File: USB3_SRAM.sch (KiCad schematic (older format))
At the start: 33 parts

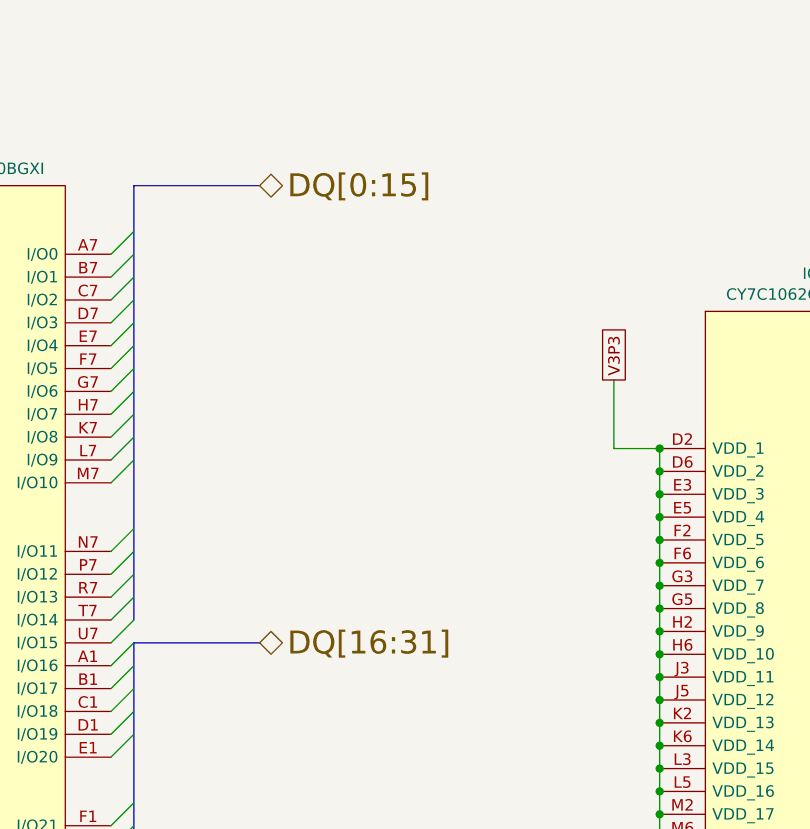
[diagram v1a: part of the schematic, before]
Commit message: Added nets for fx3 usb3 cct from fpga
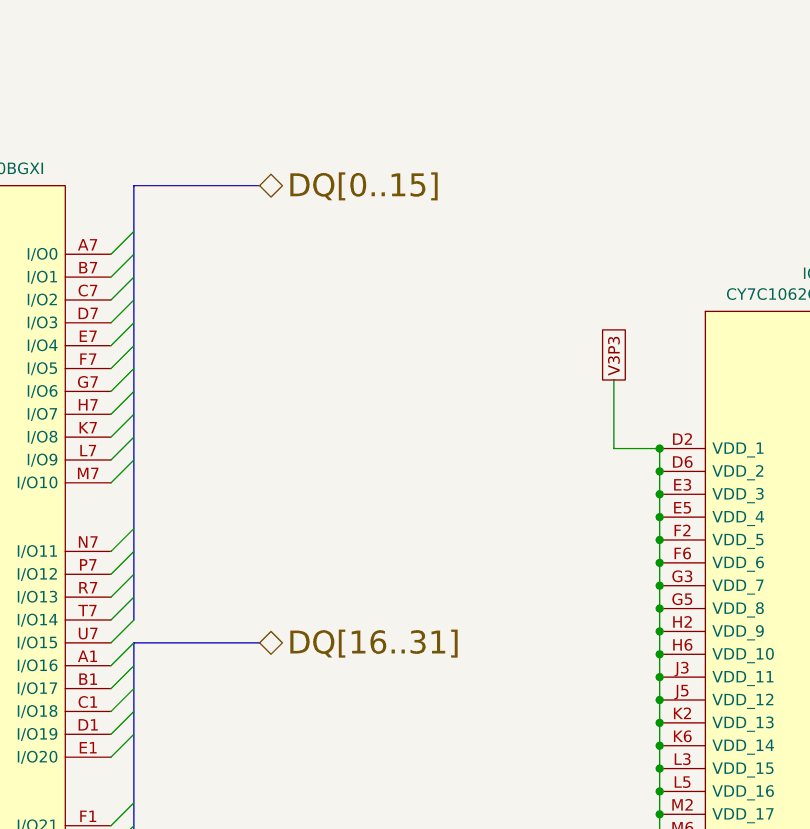
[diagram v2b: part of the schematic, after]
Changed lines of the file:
@@
 $Descr A4 11693 8268
 encoding utf-8
-Sheet 9 22
+Sheet 15 22
 Title ""
 Date ""
@@
 	6800 3700 7350 3700
 Text HLabel 7350 1700 2    100  BiDi ~ 0
-DQ[0:15]
+DQ[0..15]
 Text HLabel 7350 3700 2    100  BiDi ~ 0
-DQ[16:31]
+DQ[16..31]
 $Comp
 L power:GNDD #PWR?

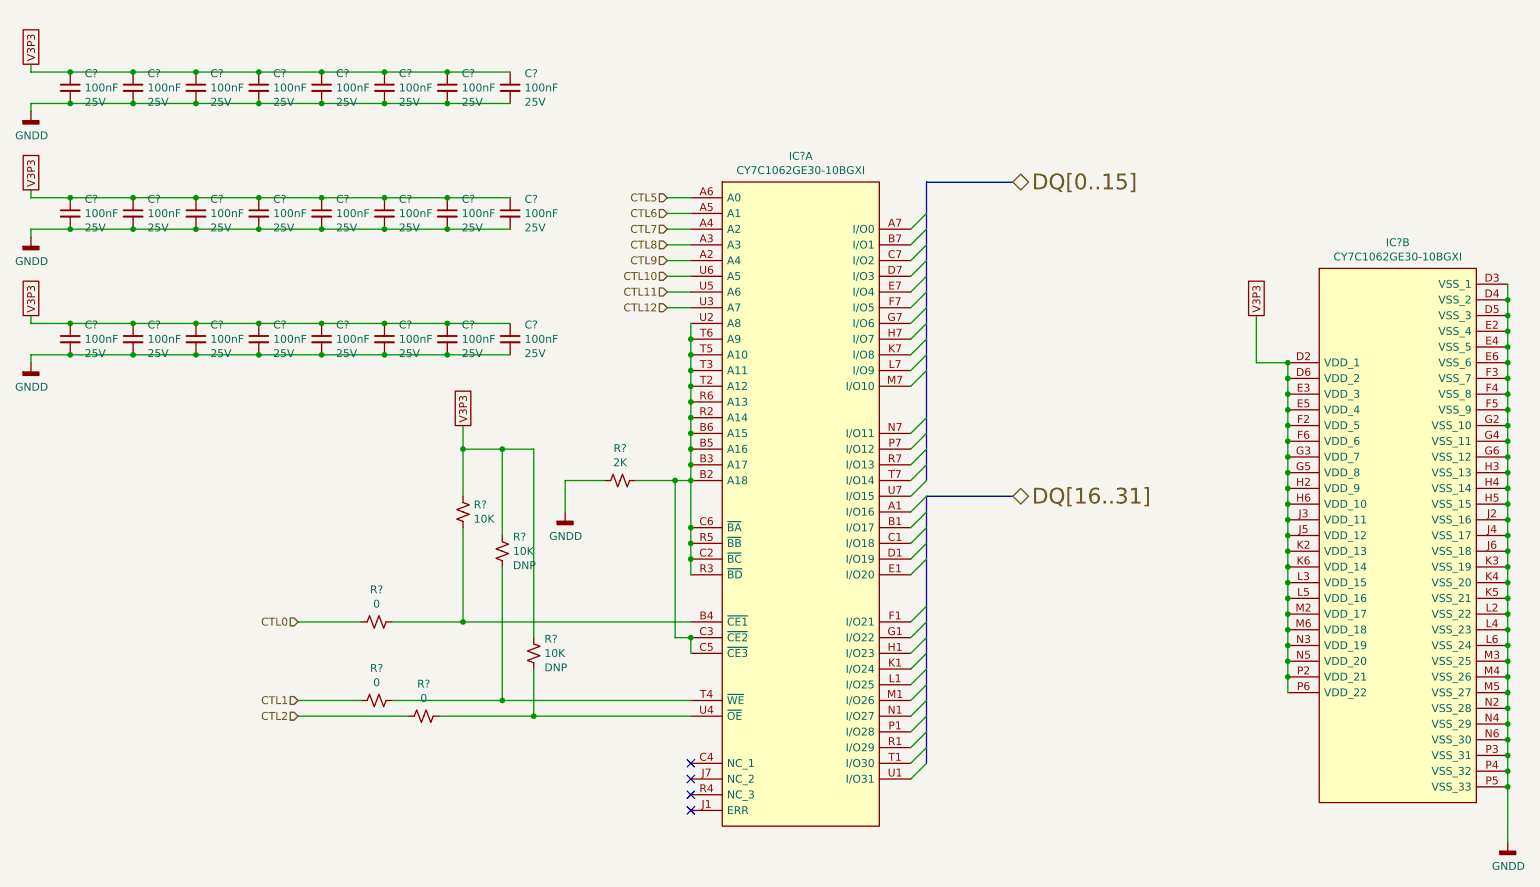
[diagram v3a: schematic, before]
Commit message: PCB created and schematics annotated High speed connections added to the BTB
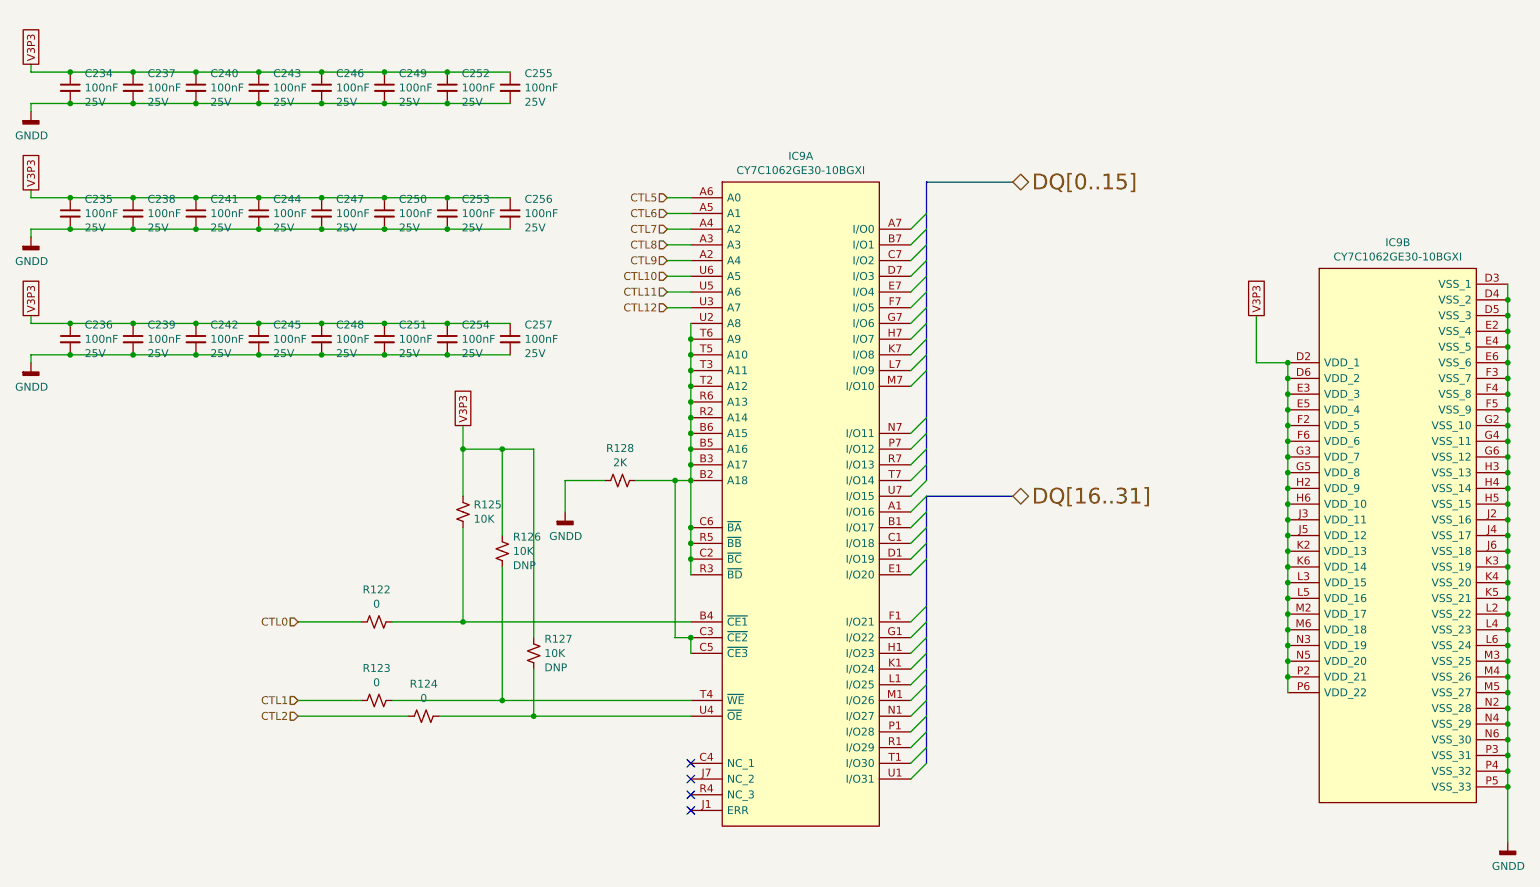
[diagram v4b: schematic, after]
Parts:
- gave numbers to parts that had none: 32

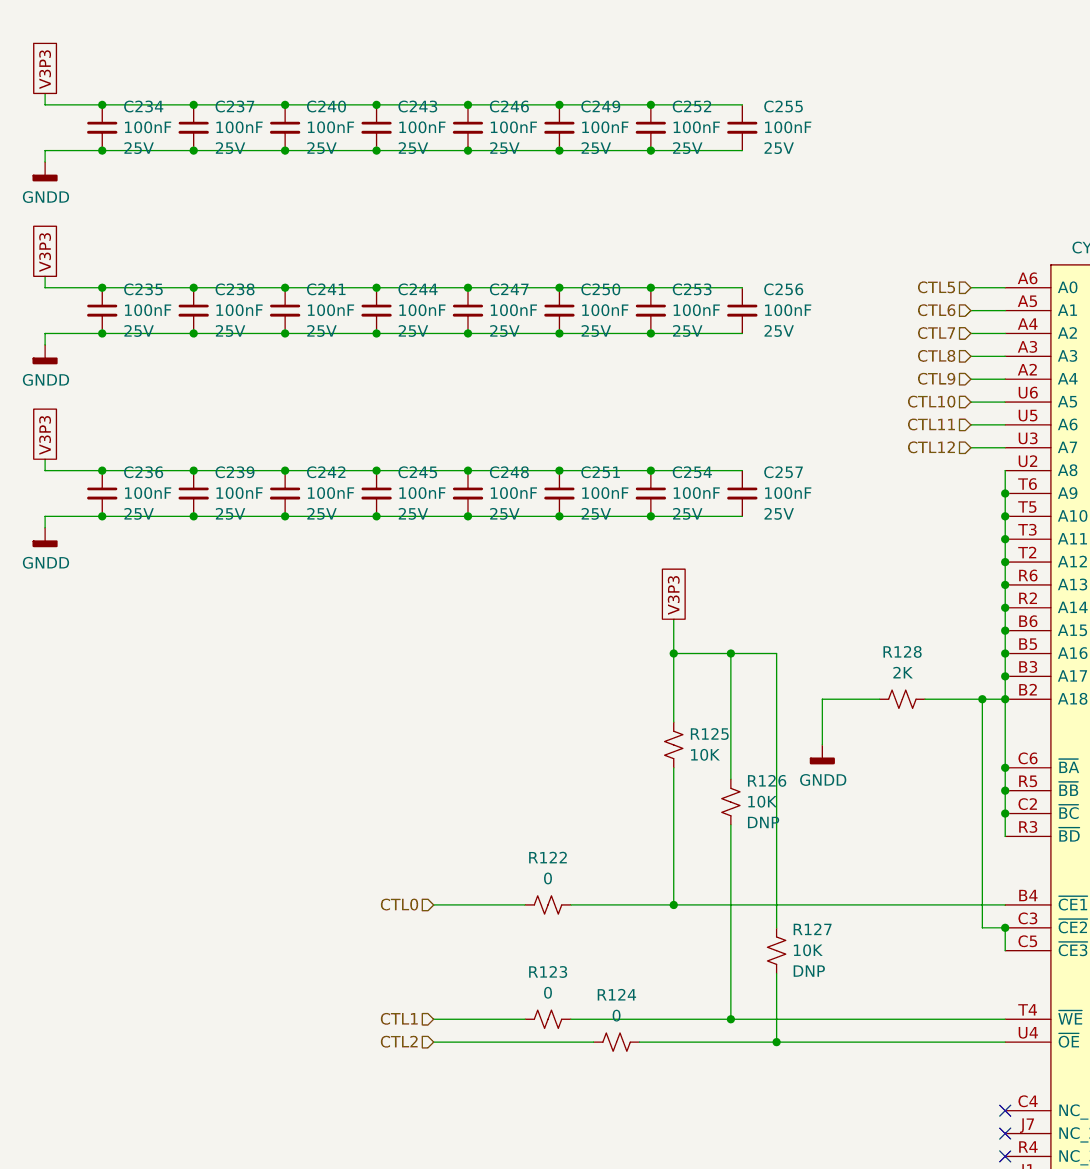
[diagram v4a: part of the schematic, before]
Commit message: Corrected PCB import errors
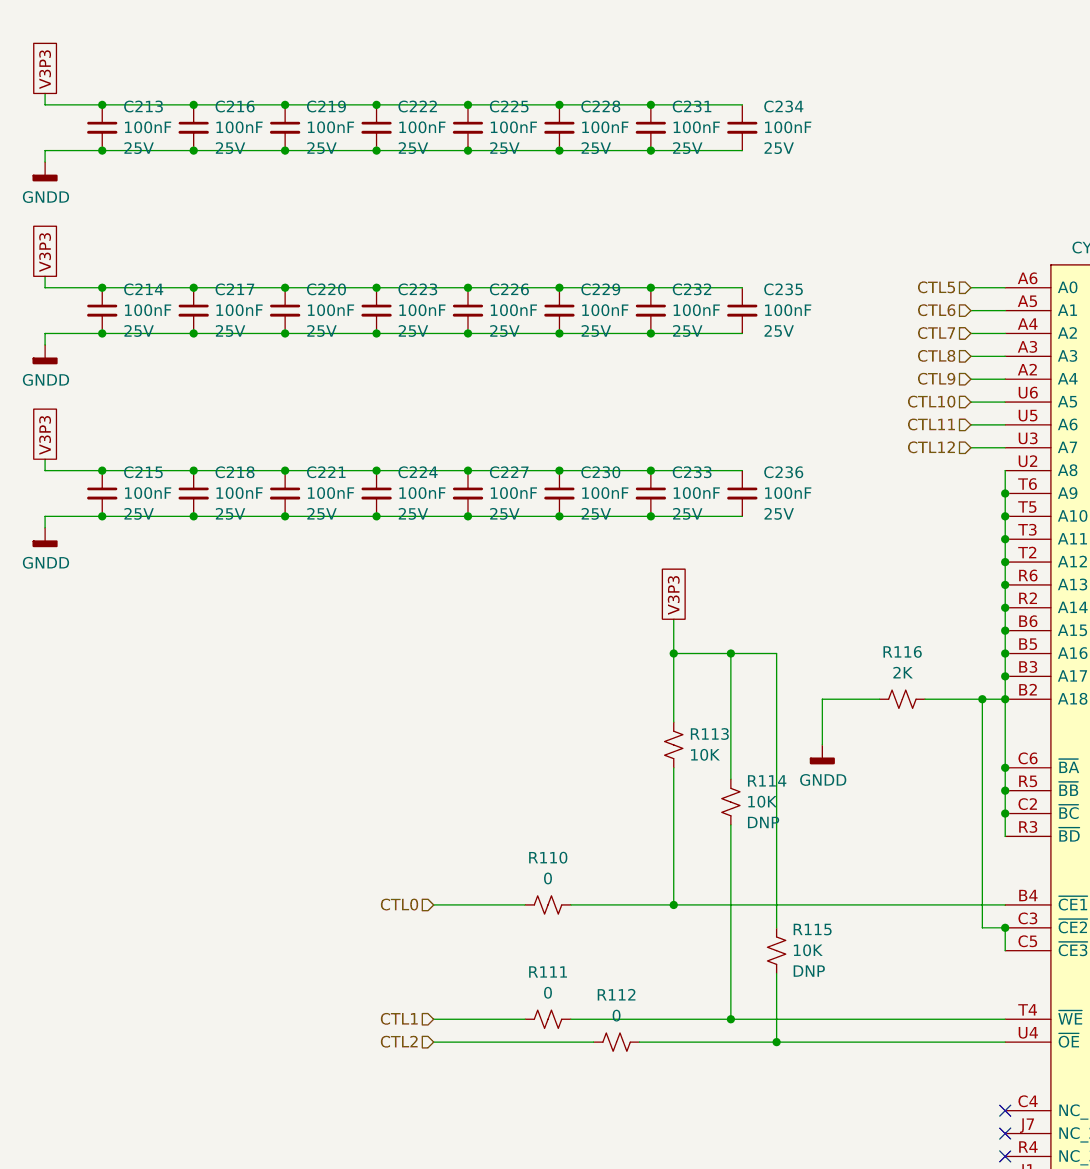
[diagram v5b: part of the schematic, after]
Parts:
- renumbered C234 to C213, C235 to C214, C236 to C215, C237 to C216, C238 to C217, C239 to C218, C240 to C219, C241 to C220, C242 to C221, C243 to C222, C244 to C223, C245 to C224, C246 to C225, C247 to C226, C248 to C227, C249 to C228, C250 to C229, C251 to C230, C252 to C231, C253 to C232, C254 to C233, C255 to C234, C256 to C235, C257 to C236, R122 to R110, R123 to R111, R124 to R112, R125 to R113, R126 to R114, R127 to R115, R128 to R116
